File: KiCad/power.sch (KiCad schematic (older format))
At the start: 10 parts

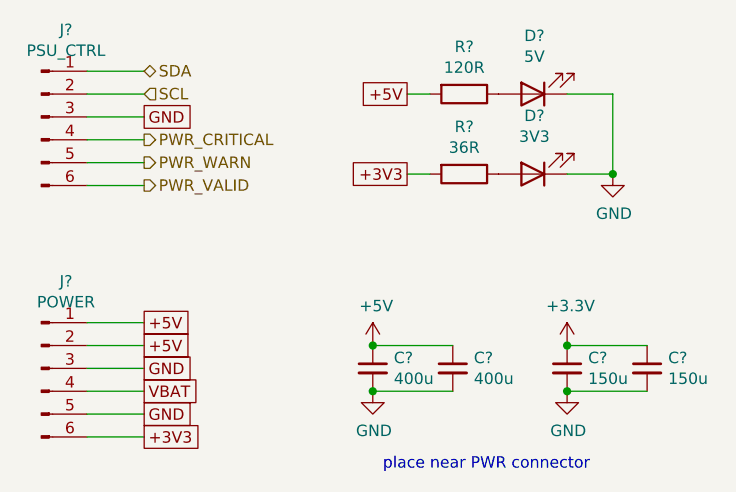
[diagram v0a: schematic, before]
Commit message: Finalized schematic and created S/F associations
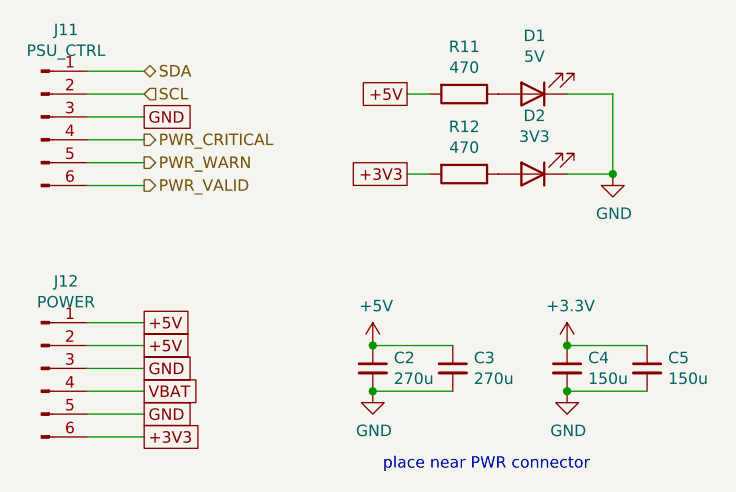
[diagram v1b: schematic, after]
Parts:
- C2, C3: renamed from C?; value 400u -> 270u; footprint (none) -> Capacitor_SMD:C_Elec_8x6.2
- C4, C5: renamed from C?; footprint (none) -> Capacitor_SMD:C_Elec_6.3x5.8
- D1, D2: renamed from D?; footprint (none) -> LED_SMD:LED_0603_1608Metric_Pad1.05x0.95mm_HandSolder
- J11: renamed from J?; footprint (none) -> Connector_JST:JST_SH_BM06B-SRSS-TB_1x06-1MP_P1.00mm_Vertical
- J12: renamed from J?; footprint (none) -> Connector_JST:JST_PH_S6B-PH-K_1x06_P2.00mm_Horizontal
- R11: renamed from R?; value 120R -> 470; footprint (none) -> Resistor_SMD:R_0603_1608Metric_Pad1.05x0.95mm_HandSolder
- R12: renamed from R?; value 36R -> 470; footprint (none) -> Resistor_SMD:R_0603_1608Metric_Pad1.05x0.95mm_HandSolder
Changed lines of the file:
@@
 $EndDescr
 $Comp
-L Device:R R?
+L Device:R R11
 U 1 1 5FCCE89D
 P 3000 1250
-F 0 "R?" V 2793 1250 50  0000 C CNN
-F 1 "120R" V 2884 1250 50  0000 C CNN
-F 2 "" V 2930 1250 50  0001 C CNN
+F 0 "R11" V 2793 1250 50  0000 C CNN
+F 1 "470" V 2884 1250 50  0000 C CNN
+F 2 "Resistor_SMD:R_0603_1608Metric_Pad1.05x0.95mm_HandSolder" V 2930 1250 50  0001 C CNN
 F 3 "~" H 3000 1250 50  0001 C CNN
 	1    3000 1250
@@
 	3650 1250 3650 1600
 $Comp
-L power:GND #PWR?
+L power:GND #PWR0121
 U 1 1 5FCC5254
 P 3650 1600
-F 0 "#PWR?" H 3650 1350 50  0001 C CNN
+F 0 "#PWR0121" H 3650 1350 50  0001 C CNN
 F 1 "GND" H 3655 1427 50  0000 C CNN
 F 2 "" H 3650 1600 50  0001 C CNN
@@
 $EndComp
 $Comp
-L Device:R R?
+L Device:R R12
 U 1 1 5FCCEB98
 P 3000 1600
-F 0 "R?" V 2793 1600 50  0000 C CNN
-F 1 "36R" V 2884 1600 50  0000 C CNN
-F 2 "" V 2930 1600 50  0001 C CNN
+F 0 "R12" V 2793 1600 50  0000 C CNN
+F 1 "470" V 2884 1600 50  0000 C CNN
+F 2 "Resistor_SMD:R_0603_1608Metric_Pad1.05x0.95mm_HandSolder" V 2930 1600 50  0001 C CNN
 F 3 "~" H 3000 1600 50  0001 C CNN
 	1    3000 1600
@@
 	3450 1250 3650 1250
 $Comp
-L Device:LED D?
+L Device:LED D2
 U 1 1 5FCC2F82
 P 3300 1600
-F 0 "D?" H 3293 1345 50  0000 C CNN
+F 0 "D2" H 3293 1345 50  0000 C CNN
 F 1 "3V3" H 3293 1436 50  0000 C CNN
-F 2 "" H 3300 1600 50  0001 C CNN
+F 2 "LED_SMD:LED_0603_1608Metric_Pad1.05x0.95mm_HandSolder" H 3300 1600 50  0001 C CNN
 F 3 "~" H 3300 1600 50  0001 C CNN
 	1    3300 1600
@@
 $EndComp
 $Comp
-L Device:LED D?
+L Device:LED D1
 U 1 1 5FCC09ED
 P 3300 1250
-F 0 "D?" H 3293 995 50  0000 C CNN
+F 0 "D1" H 3293 995 50  0000 C CNN
 F 1 "5V" H 3293 1086 50  0000 C CNN
-F 2 "" H 3300 1250 50  0001 C CNN
+F 2 "LED_SMD:LED_0603_1608Metric_Pad1.05x0.95mm_HandSolder" H 3300 1250 50  0001 C CNN
 F 3 "~" H 3300 1250 50  0001 C CNN
 	1    3300 1250
@@
 Connection ~ 3450 2350
 $Comp
-L power:+3.3V #PWR?
+L power:+3.3V #PWR0122
 U 1 1 5FCB68E8
 P 3450 2350
-F 0 "#PWR?" H 3450 2200 50  0001 C CNN
+F 0 "#PWR0122" H 3450 2200 50  0001 C CNN
 F 1 "+3.3V" H 3465 2523 50  0000 C CNN
 F 2 "" H 3450 2350 50  0001 C CNN
@@
 Connection ~ 3450 2550
 $Comp
-L power:GND #PWR?
+L power:GND #PWR0123
 U 1 1 5FCB553C
 P 3450 2550
-F 0 "#PWR?" H 3450 2300 50  0001 C CNN
+F 0 "#PWR0123" H 3450 2300 50  0001 C CNN
 F 1 "GND" H 3455 2377 50  0000 C CNN
 F 2 "" H 3450 2550 50  0001 C CNN
@@
 Connection ~ 2600 2550
 $Comp
-L power:GND #PWR?
+L power:GND #PWR0124
 U 1 1 5FCB4F91
 P 2600 2550
-F 0 "#PWR?" H 2600 2300 50  0001 C CNN
+F 0 "#PWR0124" H 2600 2300 50  0001 C CNN
 F 1 "GND" H 2605 2377 50  0000 C CNN
 F 2 "" H 2600 2550 50  0001 C CNN
@@
 Connection ~ 2600 2350
 $Comp
-L power:+5V #PWR?
+L power:+5V #PWR0125
 U 1 1 5FCB4AB5
 P 2600 2350
-F 0 "#PWR?" H 2600 2200 50  0001 C CNN
+F 0 "#PWR0125" H 2600 2200 50  0001 C CNN
 F 1 "+5V" H 2615 2523 50  0000 C CNN
 F 2 "" H 2600 2350 50  0001 C CNN
@@
 	2600 2350 2950 2350
 $Comp
-L Device:C_Small C?
+L Device:C_Small C5
 U 1 1 5FCB2DDD
 P 3800 2450
-F 0 "C?" H 3892 2496 50  0000 L CNN
+F 0 "C5" H 3892 2496 50  0000 L CNN
 F 1 "150u" H 3892 2405 50  0000 L CNN
-F 2 "" H 3800 2450 50  0001 C CNN
+F 2 "Capacitor_SMD:C_Elec_6.3x5.8" H 3800 2450 50  0001 C CNN
 F 3 "~" H 3800 2450 50  0001 C CNN
 	1    3800 2450
@@
 $EndComp
 $Comp
-L Device:C_Small C?
+L Device:C_Small C4
 U 1 1 5FCB2044
 P 3450 2450
-F 0 "C?" H 3542 2496 50  0000 L CNN
+F 0 "C4" H 3542 2496 50  0000 L CNN
 F 1 "150u" H 3542 2405 50  0000 L CNN
-F 2 "" H 3450 2450 50  0001 C CNN
+F 2 "Capacitor_SMD:C_Elec_6.3x5.8" H 3450 2450 50  0001 C CNN
 F 3 "~" H 3450 2450 50  0001 C CNN
 	1    3450 2450
@@
 $EndComp
 $Comp
-L Device:C_Small C?
+L Device:C_Small C3
 U 1 1 5FCB146F
 P 2950 2450
-F 0 "C?" H 3042 2496 50  0000 L CNN
-F 1 "400u" H 3042 2405 50  0000 L CNN
-F 2 "" H 2950 2450 50  0001 C CNN
+F 0 "C3" H 3042 2496 50  0000 L CNN
+F 1 "270u" H 3042 2405 50  0000 L CNN
+F 2 "Capacitor_SMD:C_Elec_8x6.2" H 2950 2450 50  0001 C CNN
 F 3 "~" H 2950 2450 50  0001 C CNN
 	1    2950 2450
@@
 $EndComp
 $Comp
-L Device:C_Small C?
+L Device:C_Small C2
 U 1 1 5FCB0A51
 P 2600 2450
-F 0 "C?" H 2692 2496 50  0000 L CNN
-F 1 "400u" H 2692 2405 50  0000 L CNN
-F 2 "" H 2600 2450 50  0001 C CNN
+F 0 "C2" H 2692 2496 50  0000 L CNN
+F 1 "270u" H 2692 2405 50  0000 L CNN
+F 2 "Capacitor_SMD:C_Elec_8x6.2" H 2600 2450 50  0001 C CNN
 F 3 "~" H 2600 2450 50  0001 C CNN
 	1    2600 2450
@@
 PWR_CRITICAL
 $Comp
-L Connector:Conn_01x06_Male J?
+L Connector:Conn_01x06_Male J11
 U 1 1 5FCAB8A7
 P 1150 1350
-F 0 "J?" H 1258 1731 50  0000 C CNN
+F 0 "J11" H 1258 1731 50  0000 C CNN
 F 1 "PSU_CTRL" H 1258 1640 50  0000 C CNN
-F 2 "" H 1150 1350 50  0001 C CNN
+F 2 "Connector_JST:JST_SH_BM06B-SRSS-TB_1x06-1MP_P1.00mm_Vertical" H 1150 1350 50  0001 C CNN
 F 3 "~" H 1150 1350 50  0001 C CNN
 	1    1150 1350
@@
 	1600 1250 1350 1250
 $Comp
-L Connector:Conn_01x06_Male J?
+L Connector:Conn_01x06_Male J12
 U 1 1 5FCAA2E0
 P 1150 2450
-F 0 "J?" H 1258 2831 50  0000 C CNN
+F 0 "J12" H 1258 2831 50  0000 C CNN
 F 1 "POWER" H 1258 2740 50  0000 C CNN
-F 2 "" H 1150 2450 50  0001 C CNN
+F 2 "Connector_JST:JST_PH_S6B-PH-K_1x06_P2.00mm_Horizontal" H 1150 2450 50  0001 C CNN
 F 3 "~" H 1150 2450 50  0001 C CNN
 	1    1150 2450

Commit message: Done some stuff
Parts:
- removed C2, C3: 270u, Capacitor_SMD:C_Elec_8x6.2, symbol Device:C_Small
- removed C4, C5: 150u, Capacitor_SMD:C_Elec_6.3x5.8, symbol Device:C_Small
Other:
- note removed: "place near PWR connector"
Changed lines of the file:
@@
 	-1   0    0    1
-$EndComp
-Text Notes 3550 2900 2    50   ~ 0
-place near PWR connector
-Connection ~ 3450 2350
-$Comp
-L power:+3.3V #PWR0122
-U 1 1 5FCB68E8
-P 3450 2350
-F 0 "#PWR0122" H 3450 2200 50  0001 C CNN
-F 1 "+3.3V" H 3465 2523 50  0000 C CNN
-F 2 "" H 3450 2350 50  0001 C CNN
-F 3 "" H 3450 2350 50  0001 C CNN
-	1    3450 2350
-	1    0    0    -1
-$EndComp
-Connection ~ 3450 2550
-$Comp
-L power:GND #PWR0123
-U 1 1 5FCB553C
-P 3450 2550
-F 0 "#PWR0123" H 3450 2300 50  0001 C CNN
-F 1 "GND" H 3455 2377 50  0000 C CNN
-F 2 "" H 3450 2550 50  0001 C CNN
-F 3 "" H 3450 2550 50  0001 C CNN
-	1    3450 2550
-	1    0    0    -1
-$EndComp
-Connection ~ 2600 2550
-$Comp
-L power:GND #PWR0124
-U 1 1 5FCB4F91
-P 2600 2550
-F 0 "#PWR0124" H 2600 2300 50  0001 C CNN
-F 1 "GND" H 2605 2377 50  0000 C CNN
-F 2 "" H 2600 2550 50  0001 C CNN
-F 3 "" H 2600 2550 50  0001 C CNN
-	1    2600 2550
-	1    0    0    -1
-$EndComp
-Connection ~ 2600 2350
-$Comp
-L power:+5V #PWR0125
-U 1 1 5FCB4AB5
-P 2600 2350
-F 0 "#PWR0125" H 2600 2200 50  0001 C CNN
-F 1 "+5V" H 2615 2523 50  0000 C CNN
-F 2 "" H 2600 2350 50  0001 C CNN
-F 3 "" H 2600 2350 50  0001 C CNN
-	1    2600 2350
-	1    0    0    -1
 $EndComp
 Text GLabel 1600 2250 2    50   UnSpc ~ 0
 +5V
-Wire Wire Line
-	3450 2550 3800 2550
-Wire Wire Line
-	3450 2350 3800 2350
-Wire Wire Line
-	2600 2550 2950 2550
-Wire Wire Line
-	2600 2350 2950 2350
-$Comp
-L Device:C_Small C5
-U 1 1 5FCB2DDD
-P 3800 2450
-F 0 "C5" H 3892 2496 50  0000 L CNN
-F 1 "150u" H 3892 2405 50  0000 L CNN
-F 2 "Capacitor_SMD:C_Elec_6.3x5.8" H 3800 2450 50  0001 C CNN
-F 3 "~" H 3800 2450 50  0001 C CNN
-	1    3800 2450
-	1    0    0    -1
-$EndComp
-$Comp
-L Device:C_Small C4
-U 1 1 5FCB2044
-P 3450 2450
-F 0 "C4" H 3542 2496 50  0000 L CNN
-F 1 "150u" H 3542 2405 50  0000 L CNN
-F 2 "Capacitor_SMD:C_Elec_6.3x5.8" H 3450 2450 50  0001 C CNN
-F 3 "~" H 3450 2450 50  0001 C CNN
-	1    3450 2450
-	1    0    0    -1
-$EndComp
-$Comp
-L Device:C_Small C3
-U 1 1 5FCB146F
-P 2950 2450
-F 0 "C3" H 3042 2496 50  0000 L CNN
-F 1 "270u" H 3042 2405 50  0000 L CNN
-F 2 "Capacitor_SMD:C_Elec_8x6.2" H 2950 2450 50  0001 C CNN
-F 3 "~" H 2950 2450 50  0001 C CNN
-	1    2950 2450
-	1    0    0    -1
-$EndComp
-$Comp
-L Device:C_Small C2
-U 1 1 5FCB0A51
-P 2600 2450
-F 0 "C2" H 2692 2496 50  0000 L CNN
-F 1 "270u" H 2692 2405 50  0000 L CNN
-F 2 "Capacitor_SMD:C_Elec_8x6.2" H 2600 2450 50  0001 C CNN
-F 3 "~" H 2600 2450 50  0001 C CNN
-	1    2600 2450
-	1    0    0    -1
-$EndComp
 Text GLabel 1600 2550 2    50   UnSpc ~ 0
 VBAT
